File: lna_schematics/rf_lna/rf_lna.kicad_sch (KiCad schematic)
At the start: 26 parts, among them J1 Conn_01x02_Pin, J2 Conn_Coaxial_Small, J3 Conn_Coaxial_Small, U1 L78L05_SOT89, U2 BFP640, U3 BFP640, U4 BFP640

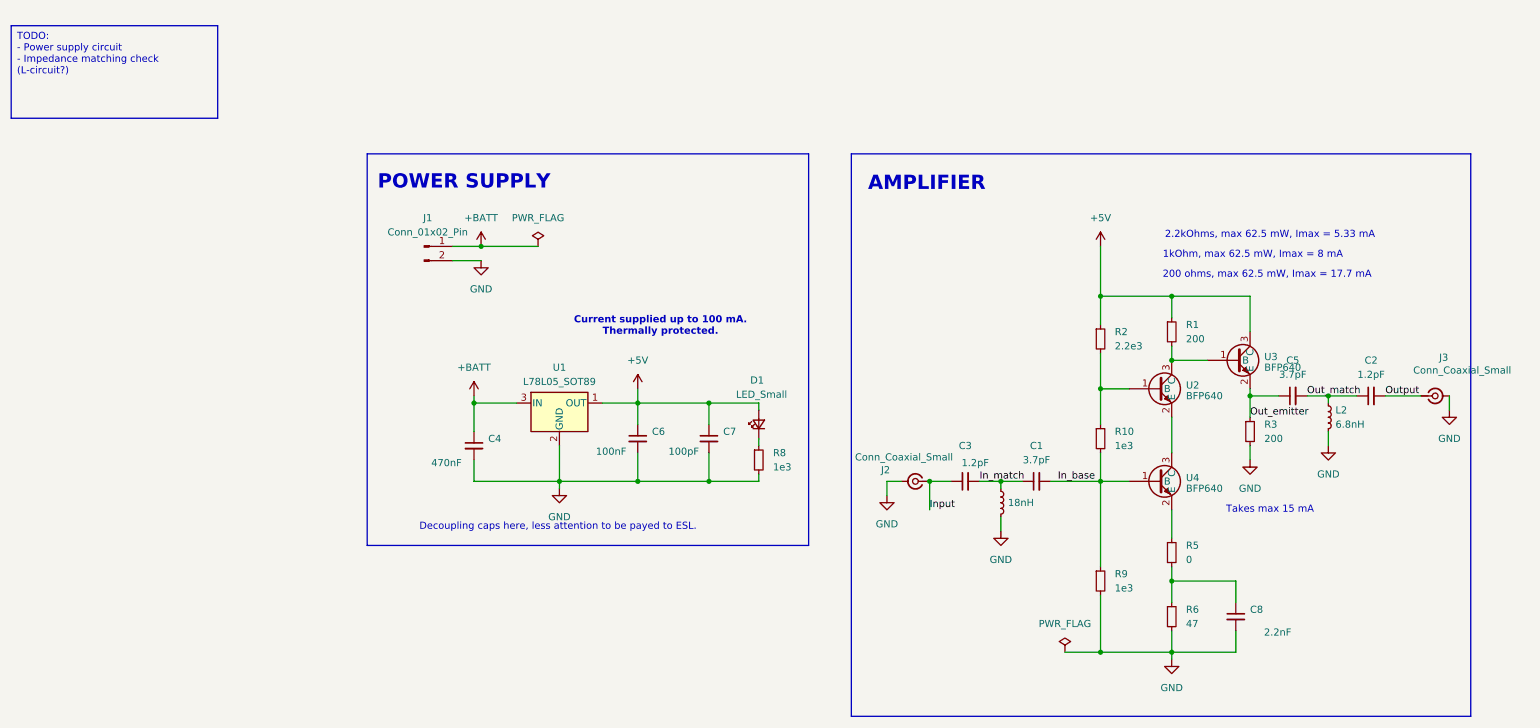
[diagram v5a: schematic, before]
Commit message: [lna_schematics] Added single-transistor LNA to schematics | TODO: update footprint and matched impedance with inductors
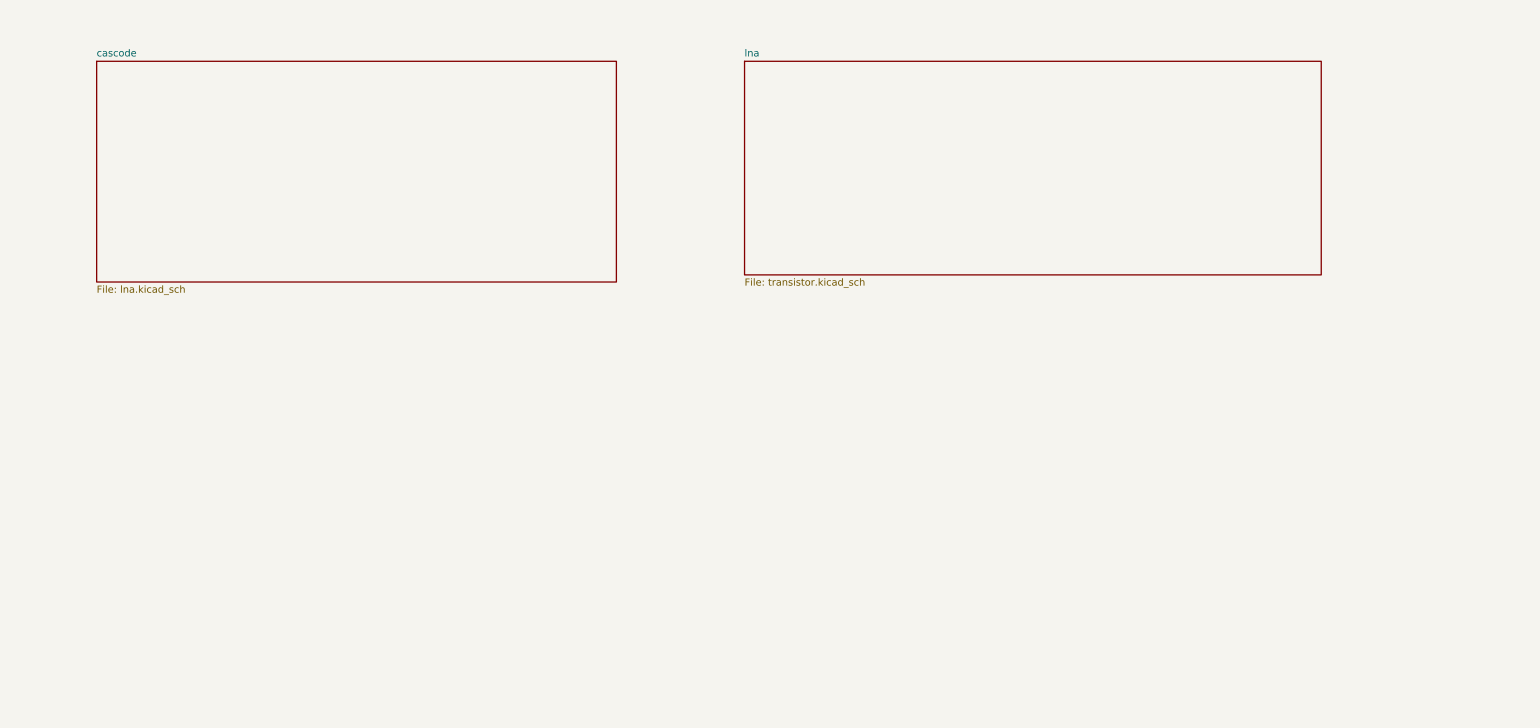
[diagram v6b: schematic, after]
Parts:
- removed C1, C5: 3.7pF, Capacitor_SMD:C_0402_1005Metric, symbol Device:C_Small
- removed C2, C3: 1.2pF, Capacitor_SMD:C_0402_1005Metric, symbol Device:C_Small
- removed C4: 470nF, Capacitor_SMD:C_0603_1608Metric, symbol Device:C_Small
- removed C6: 100nF, Capacitor_SMD:C_0402_1005Metric, symbol Device:C_Small
- removed C7: 100pF, Capacitor_SMD:C_0402_1005Metric, symbol Device:C_Small
- removed C8: 2.2nF, Capacitor_SMD:C_0805_2012Metric, symbol Device:C_Small
- removed D1: LED_Small, LED_SMD:LED_0603_1608Metric, symbol Device:LED_Small
- removed J1: Conn_01x02_Pin, Connector_Wire:SolderWire-0.25sqmm_1x02_P4.2mm_D0.65mm_OD1.7mm, symbol Connector:Conn_01x02_Pin
- removed J2, J3: Conn_Coaxial_Small, Library:SMA_Amphenol_901-143_Vertical, symbol Connector:Conn_Coaxial_Small
- removed L1: 18nH, Inductor_SMD:L_0402_1005Metric, symbol Device:L_Small
- removed L2: 6.8nH, Inductor_SMD:L_0402_1005Metric, symbol Device:L_Small
- removed R1, R3: 200, Resistor_SMD:R_0402_1005Metric, symbol Device:R_Small
- removed R10, R8, R9: 1e3, Resistor_SMD:R_0402_1005Metric, symbol Device:R_Small
- removed R2: 2.2e3, Resistor_SMD:R_0402_1005Metric, symbol Device:R_Small
- removed R5: 0, Capacitor_SMD:C_0402_1005Metric, symbol Device:R_Small
- removed R6: 47, Capacitor_SMD:C_0402_1005Metric, symbol Device:R_Small
- removed U1: L78L05_SOT89, Package_TO_SOT_SMD:SOT-89-3, symbol Regulator_Linear:L78L05_SOT89
- removed U2, U3, U4: BFP640, Library:BFP640, symbol rf_lna:BFP640
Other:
- added sheet cascode (lna.kicad_sch)
- added sheet lna (transistor.kicad_sch)
- note removed: "1kOhm, max 62.5 mW, Imax = 8 mA"
- note removed: "2.2kOhms, max 62.5 mW, Imax = 5.33 mA"
- note removed: "200 ohms, max 62.5 mW, Imax = 17.7 mA"
- note removed: "AMPLIFIER"
- note removed: "Current supplied up to 100 mA. Thermally protected."
- note removed: "Decoupling caps here, less attention to be payed to ESL."
- note removed: "POWER SUPPLY"
- note removed: "Takes max 15 mA"

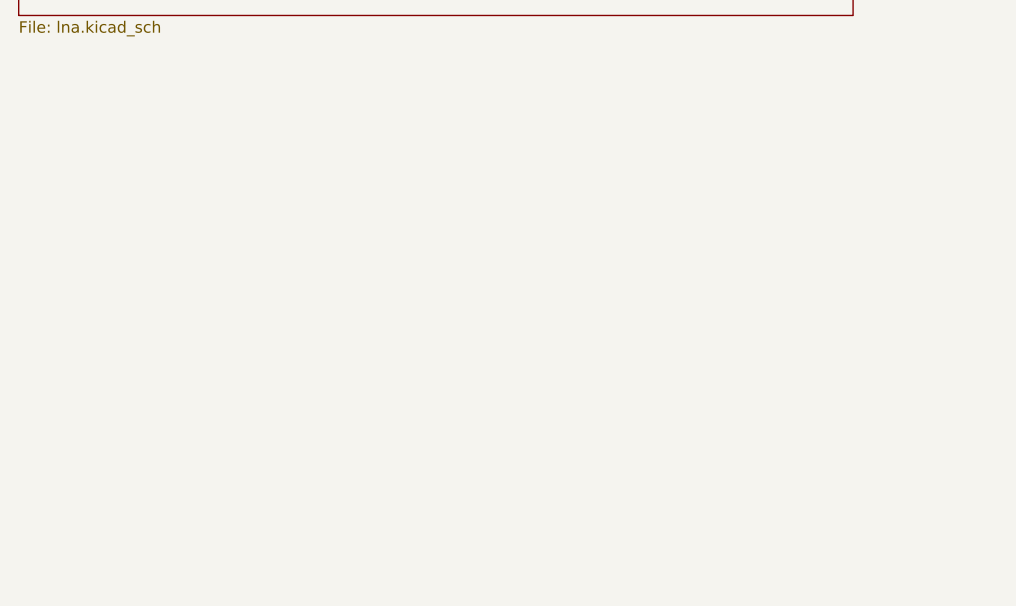
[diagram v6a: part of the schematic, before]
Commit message: [kicad] Did placement of lna components, added antenna | TODO: connect traces, add extra trace for impedance check, add antenna
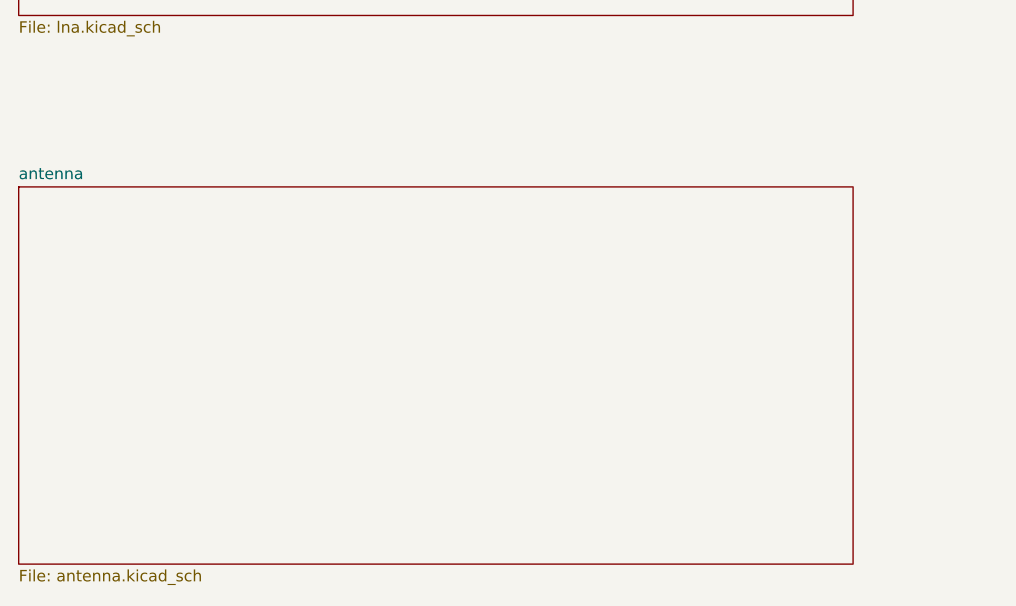
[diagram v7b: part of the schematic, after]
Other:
- added sheet antenna (antenna.kicad_sch)
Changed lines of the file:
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@@
+	)
+	(sheet
+		(at 27.94 101.6)
+		(size 92.71 41.91)
+		(fields_autoplaced yes)
+		(stroke
+			(width 0.1524)
+			(type solid)
+		)
+		(fill
+			(color 0 0 0 0.0000)
+		)
+		(property "Sheetname" "antenna"
+			(at 27.94 100.8884 0)
+			(effects
+				(font
+					(size 1.27 1.27)
+				)
+				(justify left bottom)
+			)
+		)
+		(property "Sheetfile" "antenna.kicad_sch"
+			(at 27.94 144.0946 0)
+			(effects
+				(font
+					(size 1.27 1.27)
+				)
+				(justify left top)
+			)
+		)
+		(instances
+			(project "rf_lna"
+				(path "/d07ac92b-84da-4ed3-8231-715d8aa38a44"
+					(page "4")
+				)
+			)
+		)
 	)
 	(sheet
